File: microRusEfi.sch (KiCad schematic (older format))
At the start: 44 parts, among them J4 Conn_02x05_Counter_Clockwise, U3 Molex_48_pin, U7 XC6206 3.3V

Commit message: Fix broken rescue symbol on schematic (LOGO)
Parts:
- LOGO2: symbol microRusEfi-rescue:LOGO-rusefi_Logo -> rusefi_Logo:LOGO
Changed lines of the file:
@@
 EESchema Schematic File Version 4
 LIBS:microRusEfi-cache
-EELAYER 30 0
+EELAYER 29 0
 EELAYER END
 $Descr B 17000 11000
@@
 Ign3
 $Comp
-L microRusEfi-rescue:LOGO-rusefi_Logo LOGO2
+L rusefi_Logo:LOGO LOGO2
 U 1 1 5D54AA23
 P 11425 10225

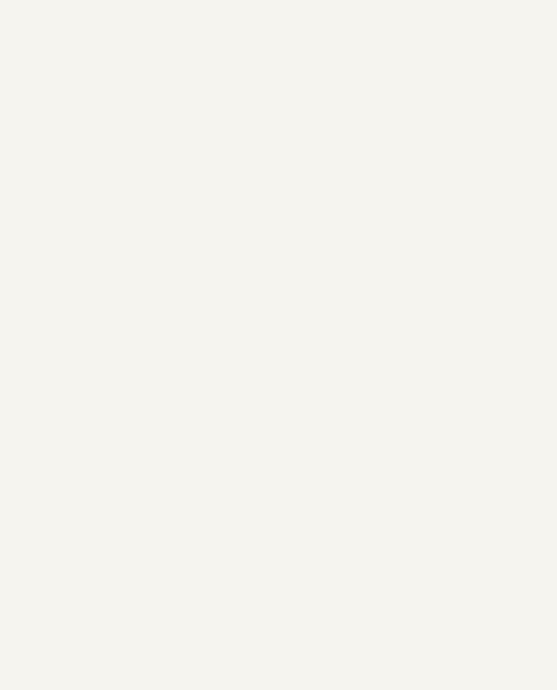
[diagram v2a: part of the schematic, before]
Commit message: Use mounting hole components on PCB instead of vias with filled zones
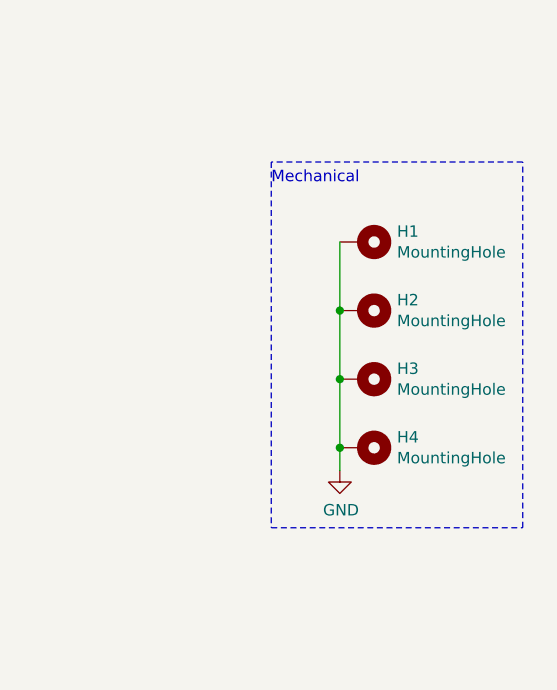
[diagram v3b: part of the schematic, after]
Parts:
- added H1, H2, H3, H4: MountingHole, Mounting_Holes:MountingHole_3.5mm_Pad_Via, symbol Mechanical:MountingHole_Pad
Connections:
- net GND: now also H1.1, H2.1, H3.1, H4.1
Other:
- note added: "Mechanical"
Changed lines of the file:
@@
 Text Label 10750 4800 0    60   ~ 12
 AV9
+$Comp
+L Mechanical:MountingHole_Pad H1
+U 1 1 5DB69683
+P 15750 8450
+F 0 "H1" V 15704 8600 50  0000 L CNN
+F 1 "MountingHole" V 15795 8600 50  0000 L CNN
+F 2 "Mounting_Holes:MountingHole_3.5mm_Pad_Via" H 15750 8450 50  0001 C CNN
+F 3 "~" H 15750 8450 50  0001 C CNN
+F 4 "DNP" H 15750 8450 50  0001 C CNN "Manufacturer"
+F 5 "DNP" H 15750 8450 50  0001 C CNN "Part #"
+F 6 "DNP" H 15750 8450 50  0001 C CNN "VEND"
+F 7 "DNP" H 15750 8450 50  0001 C CNN "VEND#"
+	1    15750 8450
+	0    1    1    0
+$EndComp
+$Comp
+L Mechanical:MountingHole_Pad H2
+U 1 1 5DB6AD9C
+P 15750 8750
+F 0 "H2" V 15704 8900 50  0000 L CNN
+F 1 "MountingHole" V 15795 8900 50  0000 L CNN
+F 2 "Mounting_Holes:MountingHole_3.5mm_Pad_Via" H 15750 8750 50  0001 C CNN
+F 3 "~" H 15750 8750 50  0001 C CNN
+F 4 "DNP" H 15750 8750 50  0001 C CNN "Manufacturer"
+F 5 "DNP" H 15750 8750 50  0001 C CNN "Part #"
+F 6 "DNP" H 15750 8750 50  0001 C CNN "VEND"
+F 7 "DNP" H 15750 8750 50  0001 C CNN "VEND#"
+	1    15750 8750
+	0    1    1    0
+$EndComp
+$Comp
+L Mechanical:MountingHole_Pad H3
+U 1 1 5DB6AFCF
+P 15750 9050
+F 0 "H3" V 15704 9200 50  0000 L CNN
+F 1 "MountingHole" V 15795 9200 50  0000 L CNN
+F 2 "Mounting_Holes:MountingHole_3.5mm_Pad_Via" H 15750 9050 50  0001 C CNN
+F 3 "~" H 15750 9050 50  0001 C CNN
+F 4 "DNP" H 15750 9050 50  0001 C CNN "Manufacturer"
+F 5 "DNP" H 15750 9050 50  0001 C CNN "Part #"
+F 6 "DNP" H 15750 9050 50  0001 C CNN "VEND"
+F 7 "DNP" H 15750 9050 50  0001 C CNN "VEND#"
+	1    15750 9050
+	0    1    1    0
+$EndComp
+$Comp
+L Mechanical:MountingHole_Pad H4
+U 1 1 5DB6B1B5
+P 15750 9350
+F 0 "H4" V 15704 9500 50  0000 L CNN
+F 1 "MountingHole" V 15795 9500 50  0000 L CNN
+F 2 "Mounting_Holes:MountingHole_3.5mm_Pad_Via" H 15750 9350 50  0001 C CNN
+F 3 "~" H 15750 9350 50  0001 C CNN
+F 4 "DNP" H 15750 9350 50  0001 C CNN "Manufacturer"
+F 5 "DNP" H 15750 9350 50  0001 C CNN "Part #"
+F 6 "DNP" H 15750 9350 50  0001 C CNN "VEND"
+F 7 "DNP" H 15750 9350 50  0001 C CNN "VEND#"
+	1    15750 9350
+	0    1    1    0
+$EndComp
+Wire Notes Line
+	15350 8100 15350 9700
+Wire Notes Line
+	15350 9700 16450 9700
+Wire Notes Line
+	16450 9700 16450 8100
+Wire Notes Line
+	16450 8100 15350 8100
+Text Notes 15350 8200 0    50   ~ 0
+Mechanical
+Wire Wire Line
+	15650 8450 15650 8750
+$Comp
+L power:GND #PWR0159
+U 1 1 5DB98A97
+P 15650 9450
+F 0 "#PWR0159" H 15650 9200 50  0001 C CNN
+F 1 "GND" H 15655 9277 50  0000 C CNN
+F 2 "" H 15650 9450 50  0001 C CNN
+F 3 "" H 15650 9450 50  0001 C CNN
+	1    15650 9450
+	1    0    0    -1
+$EndComp
+Connection ~ 15650 8750
+Wire Wire Line
+	15650 8750 15650 9050
+Connection ~ 15650 9050
+Wire Wire Line
+	15650 9050 15650 9350
+Connection ~ 15650 9350
+Wire Wire Line
+	15650 9350 15650 9450
 $EndSCHEMATC

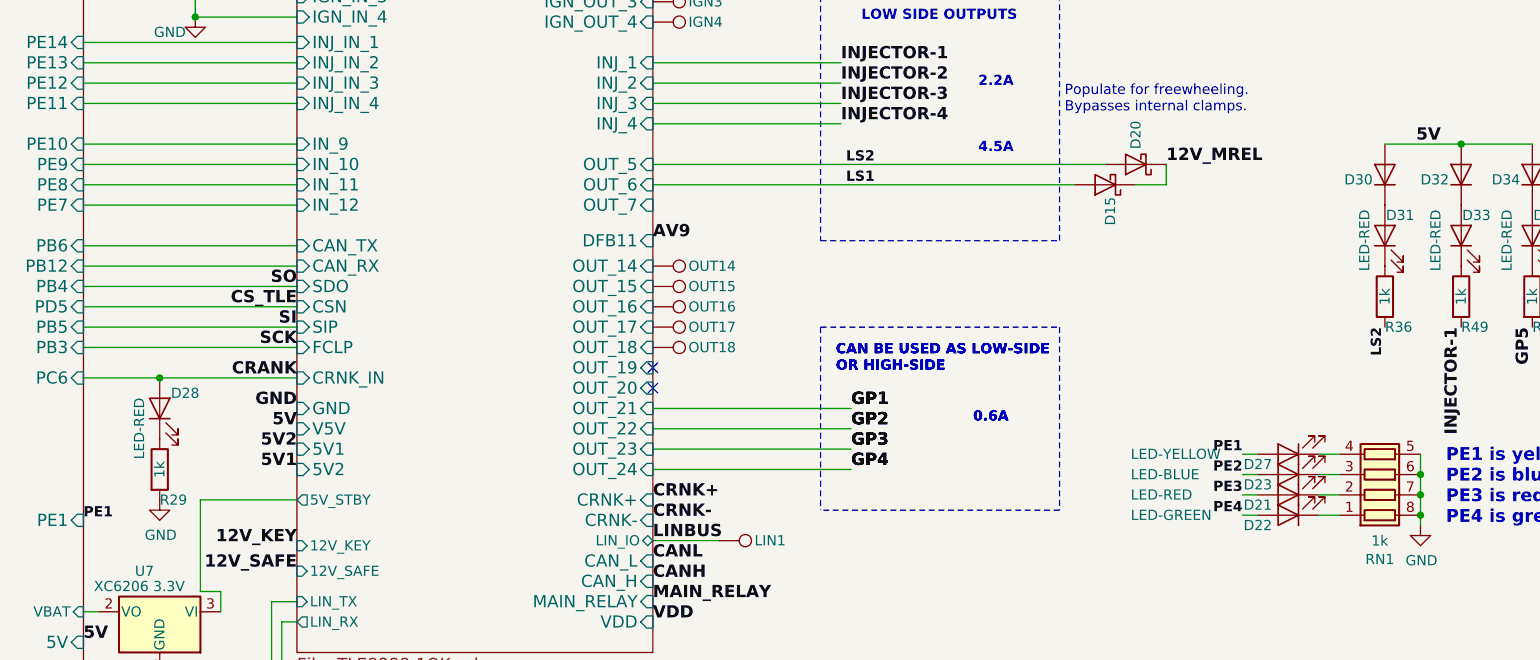
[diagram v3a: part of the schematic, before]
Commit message: Add diode and pull up on linbus. Fix some KiCAD 4.0 footprint problems
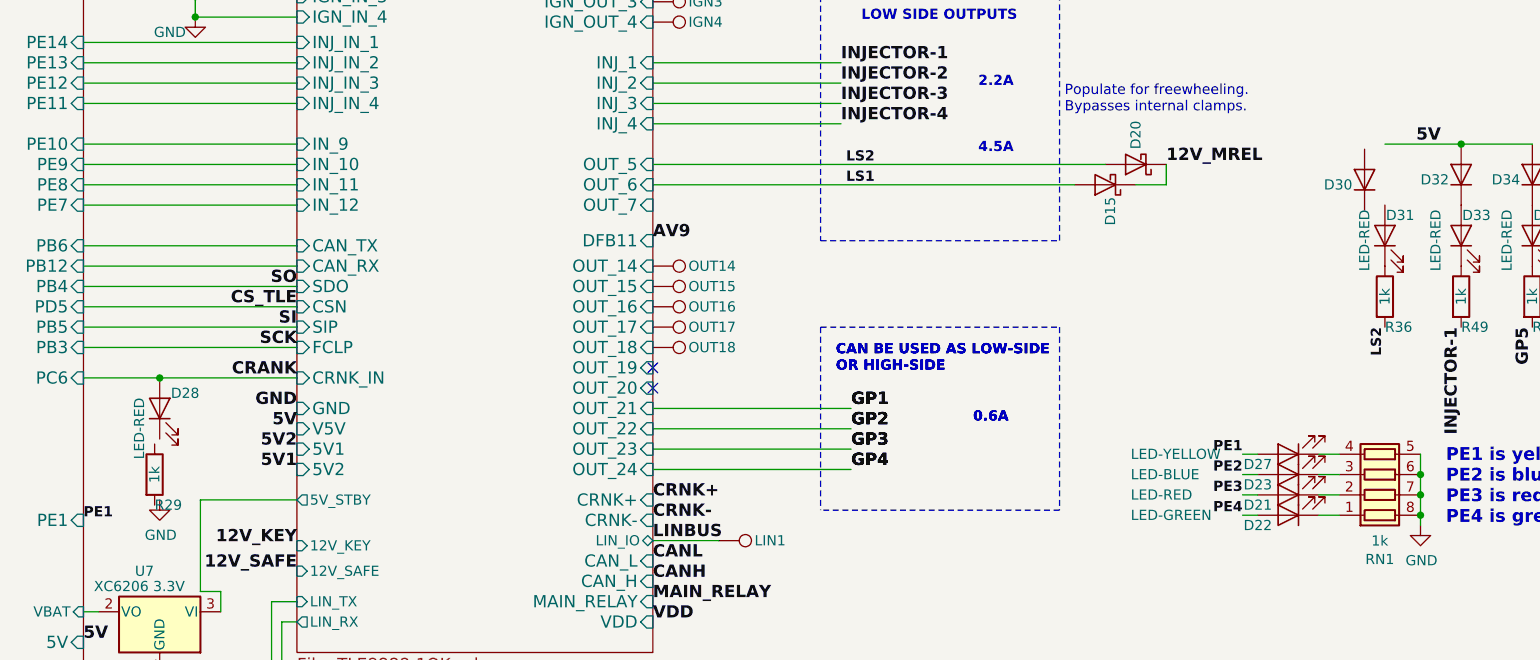
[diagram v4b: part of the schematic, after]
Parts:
- H1, H2, H3, H4: footprint Mounting_Holes:MountingHole_3.5mm_Pad_Via -> MountingHole:MountingHole_3.5mm_Pad_Via
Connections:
- net 5V: no longer D30.2 (A)
- net GND: no longer R29.2
- net at D28.1 (K): no longer R29.1
- net at D31.2 (A): no longer D30.1 (K)
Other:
- moved on the sheet: D30, R29
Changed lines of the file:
@@
 L Device:R R29
 U 1 1 5D714475
-P 8325 5925
-F 0 "R29" H 8325 5775 50  0000 L CNN
-F 1 "1k" V 8325 5925 50  0000 C CNN
-F 2 "Resistor_SMD:R_0603_1608Metric" V 8255 5925 50  0001 C CNN
-F 3 "~" H 8325 5925 50  0001 C CNN
-F 4 "StackPole" H 0   0   50  0001 C CNN "Manufacturer"
-F 5 "RMCF0603JJ1K00" H 0   0   50  0001 C CNN "Part #"
-F 6 "DIGI" H 0   0   50  0001 C CNN "VEND"
-F 7 "RMCF0603JJ1K00CT-ND" H 0   0   50  0001 C CNN "VEND#"
-F 8 "C21190" H 8325 5925 50  0001 C CNN "LCSC"
-	1    8325 5925
+P 8300 5950
+F 0 "R29" H 8300 5800 50  0000 L CNN
+F 1 "1k" V 8300 5950 50  0000 C CNN
+F 2 "Resistor_SMD:R_0603_1608Metric" V 8230 5950 50  0001 C CNN
+F 3 "~" H 8300 5950 50  0001 C CNN
+F 4 "StackPole" H -25 25  50  0001 C CNN "Manufacturer"
+F 5 "RMCF0603JJ1K00" H -25 25  50  0001 C CNN "Part #"
+F 6 "DIGI" H -25 25  50  0001 C CNN "VEND"
+F 7 "RMCF0603JJ1K00CT-ND" H -25 25  50  0001 C CNN "VEND#"
+F 8 "C21190" H 8300 5950 50  0001 C CNN "LCSC"
+	1    8300 5950
 	1    0    0    -1
 $EndComp
@@
 L Device:D D30
 U 1 1 5D907920
-P 14350 4475
-F 0 "D30" V 14325 4675 50  0000 R CNN
-F 1 "1N4148WS" H 14450 4350 50  0001 R CNN
-F 2 "Diode_SMD:D_SOD-323" H 14350 4475 50  0001 C CNN
-F 3 "~" H 14350 4475 50  0001 C CNN
-F 4 "NSR0530HT" H 3375 -200 50  0001 C CNN "Part #"
-F 5 "DIGI" H 3375 -200 50  0001 C CNN "VEND"
-F 6 "NSR0530HT1GOSCT-ND" H 3375 -200 50  0001 C CNN "VEND#"
-F 7 "ON-SEMI" H 3375 -200 50  0001 C CNN "Manufacturer"
-F 8 "C2128" H 14350 4475 50  0001 C CNN "LCSC"
-	1    14350 4475
+P 14250 4500
+F 0 "D30" V 14225 4700 50  0000 R CNN
+F 1 "1N4148WS" H 14350 4375 50  0001 R CNN
+F 2 "Diode_SMD:D_SOD-323" H 14250 4500 50  0001 C CNN
+F 3 "~" H 14250 4500 50  0001 C CNN
+F 4 "NSR0530HT" H 3275 -175 50  0001 C CNN "Part #"
+F 5 "DIGI" H 3275 -175 50  0001 C CNN "VEND"
+F 6 "NSR0530HT1GOSCT-ND" H 3275 -175 50  0001 C CNN "VEND#"
+F 7 "ON-SEMI" H 3275 -175 50  0001 C CNN "Manufacturer"
+F 8 "C2128" H 14250 4500 50  0001 C CNN "LCSC"
+	1    14250 4500
 	0    -1   -1   0
 $EndComp
@@
 F 0 "H1" V 15704 8600 50  0000 L CNN
 F 1 "MountingHole" V 15795 8600 50  0000 L CNN
-F 2 "Mounting_Holes:MountingHole_3.5mm_Pad_Via" H 15750 8450 50  0001 C CNN
+F 2 "MountingHole:MountingHole_3.5mm_Pad_Via" H 15750 8450 50  0001 C CNN
 F 3 "~" H 15750 8450 50  0001 C CNN
 F 4 "DNP" H 15750 8450 50  0001 C CNN "Manufacturer"
@@
 F 0 "H2" V 15704 8900 50  0000 L CNN
 F 1 "MountingHole" V 15795 8900 50  0000 L CNN
-F 2 "Mounting_Holes:MountingHole_3.5mm_Pad_Via" H 15750 8750 50  0001 C CNN
+F 2 "MountingHole:MountingHole_3.5mm_Pad_Via" H 15750 8750 50  0001 C CNN
 F 3 "~" H 15750 8750 50  0001 C CNN
 F 4 "DNP" H 15750 8750 50  0001 C CNN "Manufacturer"
@@
 F 0 "H3" V 15704 9200 50  0000 L CNN
 F 1 "MountingHole" V 15795 9200 50  0000 L CNN
-F 2 "Mounting_Holes:MountingHole_3.5mm_Pad_Via" H 15750 9050 50  0001 C CNN
+F 2 "MountingHole:MountingHole_3.5mm_Pad_Via" H 15750 9050 50  0001 C CNN
 F 3 "~" H 15750 9050 50  0001 C CNN
 F 4 "DNP" H 15750 9050 50  0001 C CNN "Manufacturer"
@@
 F 0 "H4" V 15704 9500 50  0000 L CNN
 F 1 "MountingHole" V 15795 9500 50  0000 L CNN
-F 2 "Mounting_Holes:MountingHole_3.5mm_Pad_Via" H 15750 9350 50  0001 C CNN
+F 2 "MountingHole:MountingHole_3.5mm_Pad_Via" H 15750 9350 50  0001 C CNN
 F 3 "~" H 15750 9350 50  0001 C CNN
 F 4 "DNP" H 15750 9350 50  0001 C CNN "Manufacturer"

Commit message: Move reset and boot buttons to be next to each other
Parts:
- TP1, TP2, TP5, TP6: footprint TestPoint:TestPoint_Pad_D4.0mm -> TestPoint:TestPoint_Pad_D2.0mm
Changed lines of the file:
@@
 F 0 "TP1" V 14400 2150 50  0000 L CNN
 F 1 "5V" V 14400 2350 50  0001 L CNN
-F 2 "TestPoint:TestPoint_Pad_D4.0mm" H 14600 1975 50  0001 C CNN
+F 2 "TestPoint:TestPoint_Pad_D2.0mm" H 14600 1975 50  0001 C CNN
 F 3 "~" H 14600 1975 50  0001 C CNN
 F 4 "DNP" H 5950 -3750 50  0001 C CNN "Part #"
@@
 F 0 "TP2" V 14400 2275 50  0000 L CNN
 F 1 "GND" H 14225 2150 50  0001 L CNN
-F 2 "TestPoint:TestPoint_Pad_D4.0mm" H 14600 2100 50  0001 C CNN
+F 2 "TestPoint:TestPoint_Pad_D2.0mm" H 14600 2100 50  0001 C CNN
 F 3 "~" H 14600 2100 50  0001 C CNN
 F 4 "DNP" H 6100 -3775 50  0001 C CNN "Part #"
@@
 F 0 "TP5" V 14400 2650 50  0000 L CNN
 F 1 "5V" V 14400 2850 50  0001 L CNN
-F 2 "TestPoint:TestPoint_Pad_D4.0mm" H 14600 2475 50  0001 C CNN
+F 2 "TestPoint:TestPoint_Pad_D2.0mm" H 14600 2475 50  0001 C CNN
 F 3 "~" H 14600 2475 50  0001 C CNN
 F 4 "DNP" H 5950 -3250 50  0001 C CNN "Part #"
@@
 F 0 "TP6" V 14400 2775 50  0000 L CNN
 F 1 "GND" H 14225 2650 50  0001 L CNN
-F 2 "TestPoint:TestPoint_Pad_D4.0mm" H 14600 2600 50  0001 C CNN
+F 2 "TestPoint:TestPoint_Pad_D2.0mm" H 14600 2600 50  0001 C CNN
 F 3 "~" H 14600 2600 50  0001 C CNN
 F 4 "DNP" H 6100 -3275 50  0001 C CNN "Part #"

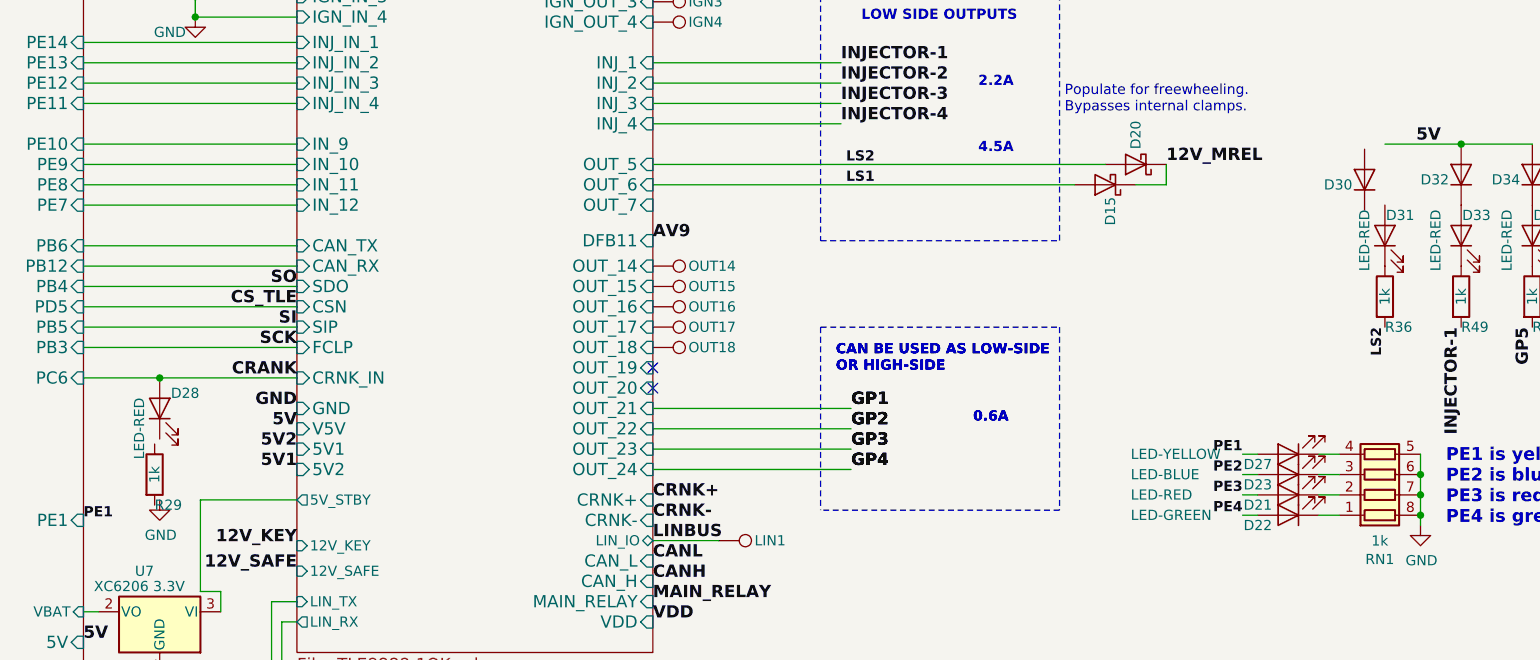
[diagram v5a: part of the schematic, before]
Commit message: Fix a few DRC errors probably introduced by me
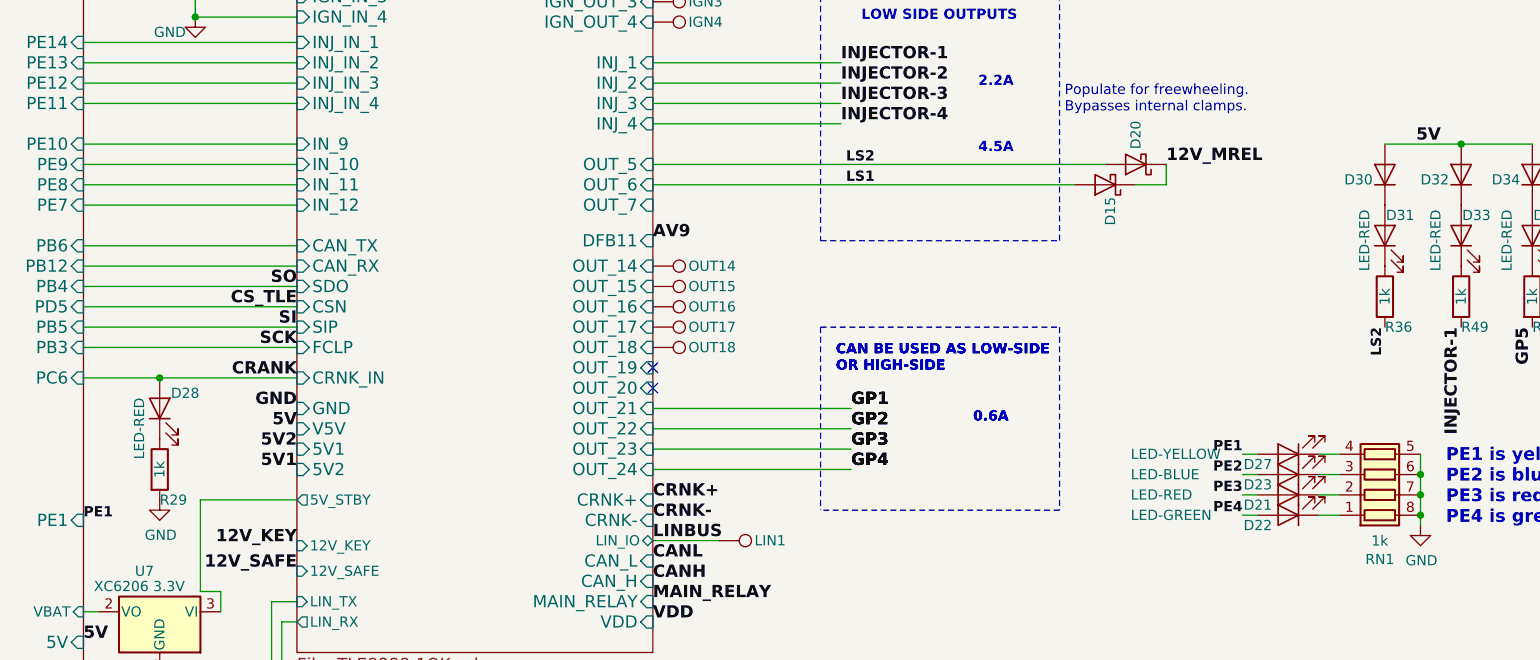
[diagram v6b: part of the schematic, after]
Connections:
- net 5V: now also D30.2 (A)
- net GND: now also R29.2
- net at D28.1 (K): now also R29.1
- net at D31.2 (A): now also D30.1 (K)
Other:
- moved on the sheet: D30, R29
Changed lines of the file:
@@
 L Device:R R29
 U 1 1 5D714475
-P 8300 5950
-F 0 "R29" H 8300 5800 50  0000 L CNN
-F 1 "1k" V 8300 5950 50  0000 C CNN
-F 2 "Resistor_SMD:R_0603_1608Metric" V 8230 5950 50  0001 C CNN
-F 3 "~" H 8300 5950 50  0001 C CNN
-F 4 "StackPole" H -25 25  50  0001 C CNN "Manufacturer"
-F 5 "RMCF0603JJ1K00" H -25 25  50  0001 C CNN "Part #"
-F 6 "DIGI" H -25 25  50  0001 C CNN "VEND"
-F 7 "RMCF0603JJ1K00CT-ND" H -25 25  50  0001 C CNN "VEND#"
-F 8 "C21190" H 8300 5950 50  0001 C CNN "LCSC"
-	1    8300 5950
+P 8325 5925
+F 0 "R29" H 8325 5775 50  0000 L CNN
+F 1 "1k" V 8325 5925 50  0000 C CNN
+F 2 "Resistor_SMD:R_0603_1608Metric" V 8255 5925 50  0001 C CNN
+F 3 "~" H 8325 5925 50  0001 C CNN
+F 4 "StackPole" H 0   0   50  0001 C CNN "Manufacturer"
+F 5 "RMCF0603JJ1K00" H 0   0   50  0001 C CNN "Part #"
+F 6 "DIGI" H 0   0   50  0001 C CNN "VEND"
+F 7 "RMCF0603JJ1K00CT-ND" H 0   0   50  0001 C CNN "VEND#"
+F 8 "C21190" H 8325 5925 50  0001 C CNN "LCSC"
+	1    8325 5925
 	1    0    0    -1
 $EndComp
@@
 L Device:D D30
 U 1 1 5D907920
-P 14250 4500
-F 0 "D30" V 14225 4700 50  0000 R CNN
-F 1 "1N4148WS" H 14350 4375 50  0001 R CNN
-F 2 "Diode_SMD:D_SOD-323" H 14250 4500 50  0001 C CNN
-F 3 "~" H 14250 4500 50  0001 C CNN
-F 4 "NSR0530HT" H 3275 -175 50  0001 C CNN "Part #"
-F 5 "DIGI" H 3275 -175 50  0001 C CNN "VEND"
-F 6 "NSR0530HT1GOSCT-ND" H 3275 -175 50  0001 C CNN "VEND#"
-F 7 "ON-SEMI" H 3275 -175 50  0001 C CNN "Manufacturer"
-F 8 "C2128" H 14250 4500 50  0001 C CNN "LCSC"
-	1    14250 4500
+P 14350 4475
+F 0 "D30" V 14325 4675 50  0000 R CNN
+F 1 "1N4148WS" H 14450 4350 50  0001 R CNN
+F 2 "Diode_SMD:D_SOD-323" H 14350 4475 50  0001 C CNN
+F 3 "~" H 14350 4475 50  0001 C CNN
+F 4 "NSR0530HT" H 3375 -200 50  0001 C CNN "Part #"
+F 5 "DIGI" H 3375 -200 50  0001 C CNN "VEND"
+F 6 "NSR0530HT1GOSCT-ND" H 3375 -200 50  0001 C CNN "VEND#"
+F 7 "ON-SEMI" H 3375 -200 50  0001 C CNN "Manufacturer"
+F 8 "C2128" H 14350 4475 50  0001 C CNN "LCSC"
+	1    14350 4475
 	0    -1   -1   0
 $EndComp
